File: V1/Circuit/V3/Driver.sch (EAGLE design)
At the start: 40 parts, among them IC1 DRV8303DCA

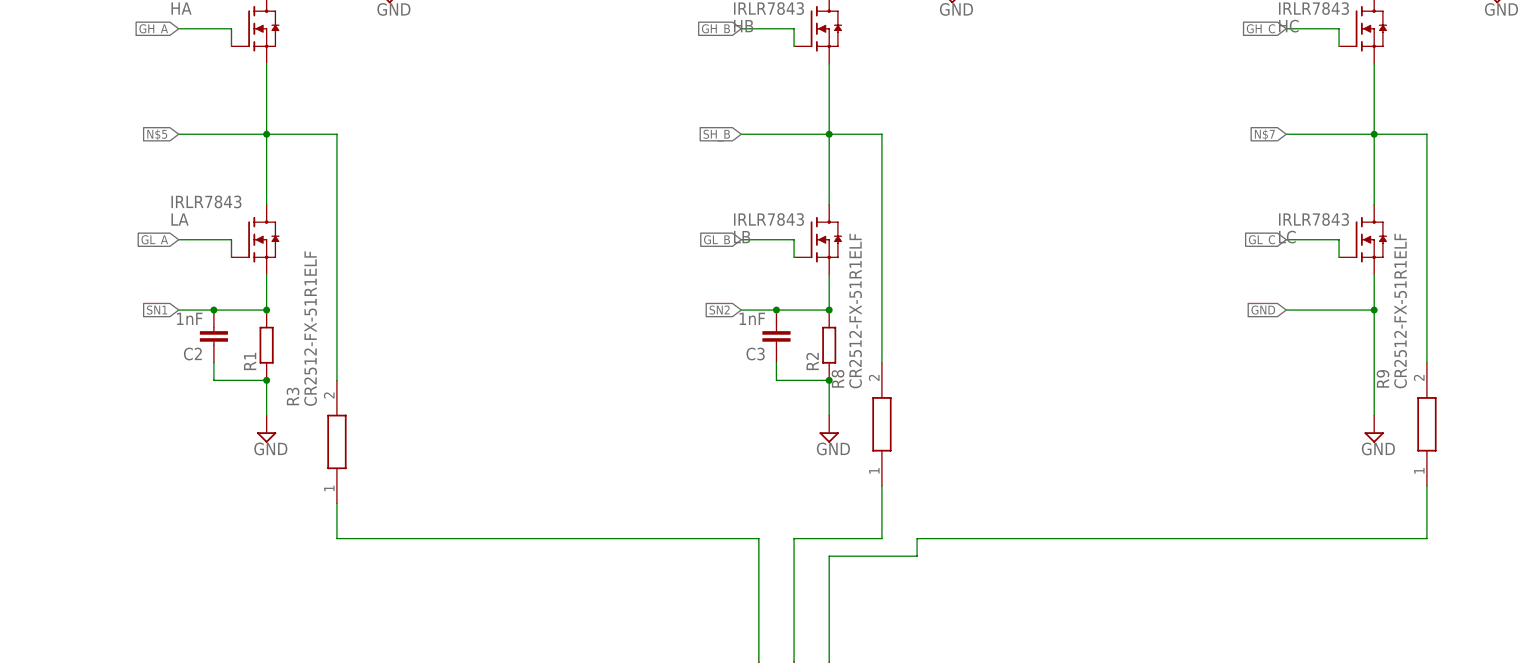
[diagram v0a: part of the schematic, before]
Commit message: Added the FOC library
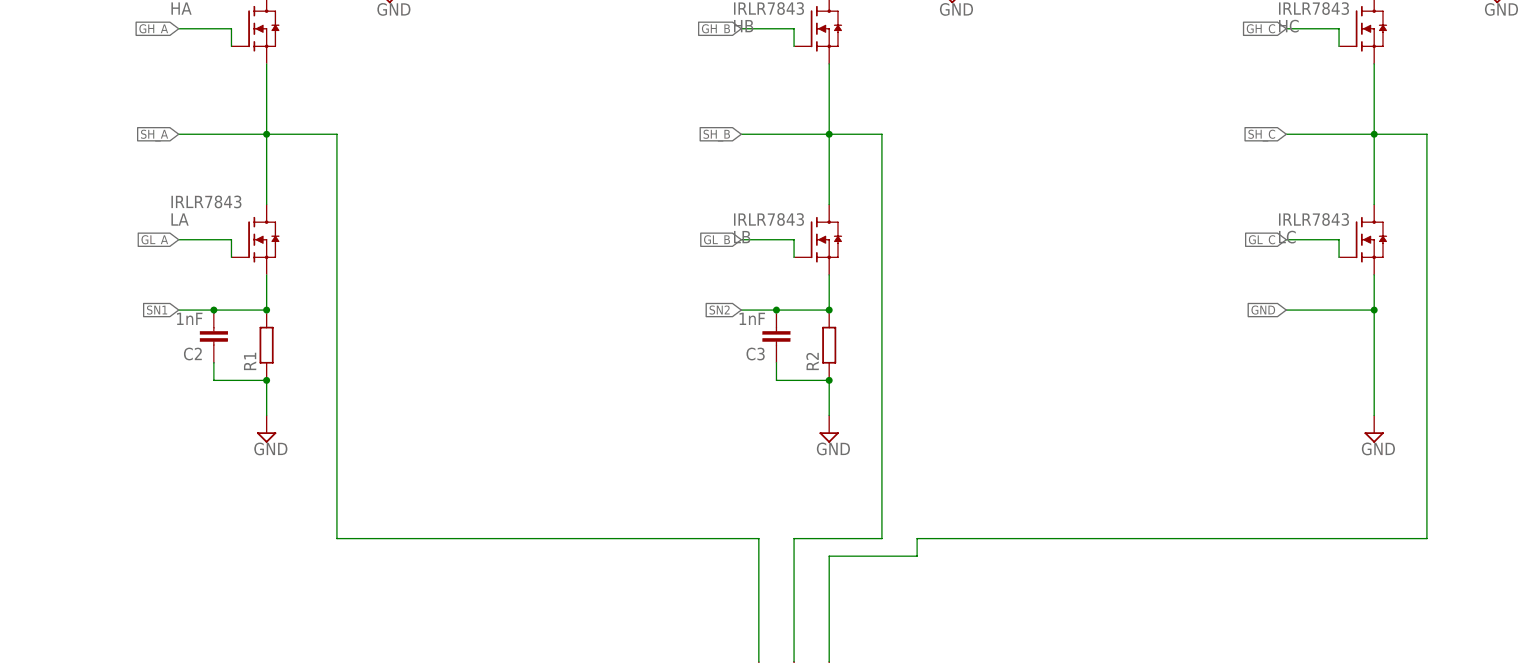
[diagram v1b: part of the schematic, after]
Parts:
- removed R3, R8, R9: CR2512-FX-51R1ELF, CR2512-FX-51R1ELF:CR2512-FX-51R1ELF
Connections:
- removed net N$5: HA.S, LA.D, R3.2
- removed net N$6: B.P, R8.1
- removed net N$7: HC.S, LC.D, R9.2
- net SH_A: now also HA.S, LA.D; no longer R3.1
- net SH_B: now also B.P; no longer R8.2
- net SH_C: now also HC.S, LC.D; no longer R9.1
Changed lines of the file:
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@@
 <part name="SUPPLY24" library="supply2" library_urn="urn:adsk.eagle:library:372" deviceset="GND" device=""/>
 <part name="C16" library="SparkFun-Capacitors" deviceset="2.2NF/2200PF" device="-0603-50V-10%" value="2.2nF"/>
-<part name="R3" library="CR2512-FX-51R1ELF" deviceset="CR2512-FX-51R1ELF" device=""/>
-<part name="R8" library="CR2512-FX-51R1ELF" deviceset="CR2512-FX-51R1ELF" device=""/>
-<part name="R9" library="CR2512-FX-51R1ELF" deviceset="CR2512-FX-51R1ELF" device=""/>
 </parts>
 <sheets>
@@
 <attribute name="NAME" x="194.564" y="91.821" size="1.778" layer="95" font="vector"/>
 <attribute name="VALUE" x="194.564" y="86.741" size="1.778" layer="96" font="vector"/>
-</instance>
-<instance part="R3" gate="G$1" x="162.56" y="-58.42" smashed="yes" rot="R90">
-<attribute name="NAME" x="156.21" y="-44.45" size="1.778" layer="95" rot="R90" align="center-left"/>
-<attribute name="VALUE" x="158.75" y="-44.45" size="1.778" layer="96" rot="R90" align="center-left"/>
-</instance>
-<instance part="R8" gate="G$1" x="241.3" y="-55.88" smashed="yes" rot="R90">
-<attribute name="NAME" x="234.95" y="-41.91" size="1.778" layer="95" rot="R90" align="center-left"/>
-<attribute name="VALUE" x="237.49" y="-41.91" size="1.778" layer="96" rot="R90" align="center-left"/>
-</instance>
-<instance part="R9" gate="G$1" x="320.04" y="-55.88" smashed="yes" rot="R90">
-<attribute name="NAME" x="313.69" y="-41.91" size="1.778" layer="95" rot="R90" align="center-left"/>
-<attribute name="VALUE" x="316.23" y="-41.91" size="1.778" layer="96" rot="R90" align="center-left"/>
 </instance>
 </instances>
@@
 <net name="SH_C" class="0">
 <segment>
+<wire x1="312.42" y1="5.08" x2="312.42" y2="-5.08" width="0.1524" layer="91"/>
+<wire x1="312.42" y1="-5.08" x2="299.72" y2="-5.08" width="0.1524" layer="91"/>
+<label x="299.72" y="-5.08" size="1.27" layer="95" rot="R180" xref="yes"/>
+<wire x1="312.42" y1="-5.08" x2="320.04" y2="-5.08" width="0.1524" layer="91"/>
+<wire x1="320.04" y1="-5.08" x2="320.04" y2="-63.5" width="0.1524" layer="91"/>
 <wire x1="320.04" y1="-63.5" x2="246.38" y2="-63.5" width="0.1524" layer="91"/>
 <wire x1="246.38" y1="-63.5" x2="246.38" y2="-66.04" width="0.1524" layer="91"/>
 <wire x1="246.38" y1="-66.04" x2="233.68" y2="-66.04" width="0.1524" layer="91"/>
 <wire x1="233.68" y1="-66.04" x2="233.68" y2="-81.28" width="0.1524" layer="91"/>
+<junction x="312.42" y="-5.08"/>
+<pinref part="HC" gate="G$1" pin="S"/>
+<pinref part="LC" gate="G$1" pin="D"/>
+<wire x1="312.42" y1="-5.08" x2="312.42" y2="-15.24" width="0.1524" layer="91"/>
 <pinref part="C" gate="1" pin="P"/>
-<wire x1="320.04" y1="-55.88" x2="320.04" y2="-63.5" width="0.1524" layer="91"/>
-<pinref part="R9" gate="G$1" pin="1"/>
 </segment>
 <segment>
@@
 <label x="220.98" y="-5.08" size="1.27" layer="95" rot="R180" xref="yes"/>
 <wire x1="233.68" y1="-5.08" x2="241.3" y2="-5.08" width="0.1524" layer="91"/>
+<wire x1="241.3" y1="-5.08" x2="241.3" y2="-63.5" width="0.1524" layer="91"/>
+<wire x1="241.3" y1="-63.5" x2="228.6" y2="-63.5" width="0.1524" layer="91"/>
+<wire x1="228.6" y1="-63.5" x2="228.6" y2="-81.28" width="0.1524" layer="91"/>
 <junction x="233.68" y="-5.08"/>
 <pinref part="HB" gate="G$1" pin="S"/>
 <pinref part="LB" gate="G$1" pin="D"/>
-<wire x1="241.3" y1="-5.08" x2="241.3" y2="-38.1" width="0.1524" layer="91"/>
-<pinref part="R8" gate="G$1" pin="2"/>
+<pinref part="B" gate="1" pin="P"/>
 </segment>
 <segment>
@@
 <net name="SH_A" class="0">
 <segment>
+<wire x1="152.4" y1="5.08" x2="152.4" y2="-5.08" width="0.1524" layer="91"/>
+<wire x1="152.4" y1="-5.08" x2="152.4" y2="-15.24" width="0.1524" layer="91"/>
+<wire x1="152.4" y1="-5.08" x2="139.7" y2="-5.08" width="0.1524" layer="91"/>
+<label x="139.7" y="-5.08" size="1.27" layer="95" rot="R180" xref="yes"/>
+<wire x1="152.4" y1="-5.08" x2="162.56" y2="-5.08" width="0.1524" layer="91"/>
+<wire x1="162.56" y1="-5.08" x2="162.56" y2="-63.5" width="0.1524" layer="91"/>
 <wire x1="162.56" y1="-63.5" x2="223.52" y2="-63.5" width="0.1524" layer="91"/>
 <wire x1="223.52" y1="-63.5" x2="223.52" y2="-81.28" width="0.1524" layer="91"/>
+<junction x="152.4" y="-5.08"/>
+<pinref part="HA" gate="G$1" pin="S"/>
+<pinref part="LA" gate="G$1" pin="D"/>
 <pinref part="A" gate="1" pin="P"/>
-<wire x1="162.56" y1="-58.42" x2="162.56" y2="-63.5" width="0.1524" layer="91"/>
-<pinref part="R3" gate="G$1" pin="1"/>
 </segment>
 <segment>
@@
 </segment>
 </net>
-<net name="N$5" class="0">
-<segment>
-<pinref part="LA" gate="G$1" pin="D"/>
-<pinref part="HA" gate="G$1" pin="S"/>
-<wire x1="152.4" y1="5.08" x2="152.4" y2="-5.08" width="0.1524" layer="91"/>
-<wire x1="152.4" y1="-5.08" x2="152.4" y2="-15.24" width="0.1524" layer="91"/>
-<wire x1="152.4" y1="-5.08" x2="139.7" y2="-5.08" width="0.1524" layer="91"/>
-<junction x="152.4" y="-5.08"/>
-<wire x1="152.4" y1="-5.08" x2="162.56" y2="-5.08" width="0.1524" layer="91"/>
-<wire x1="162.56" y1="-5.08" x2="162.56" y2="-40.64" width="0.1524" layer="91"/>
-<label x="139.7" y="-5.08" size="1.27" layer="95" rot="R180" xref="yes"/>
-<pinref part="R3" gate="G$1" pin="2"/>
-</segment>
-</net>
-<net name="N$6" class="0">
-<segment>
-<wire x1="241.3" y1="-55.88" x2="241.3" y2="-63.5" width="0.1524" layer="91"/>
-<wire x1="241.3" y1="-63.5" x2="228.6" y2="-63.5" width="0.1524" layer="91"/>
-<wire x1="228.6" y1="-63.5" x2="228.6" y2="-81.28" width="0.1524" layer="91"/>
-<pinref part="B" gate="1" pin="P"/>
-<pinref part="R8" gate="G$1" pin="1"/>
-</segment>
-</net>
-<net name="N$7" class="0">
-<segment>
-<pinref part="LC" gate="G$1" pin="D"/>
-<pinref part="HC" gate="G$1" pin="S"/>
-<wire x1="312.42" y1="5.08" x2="312.42" y2="-5.08" width="0.1524" layer="91"/>
-<wire x1="312.42" y1="-5.08" x2="299.72" y2="-5.08" width="0.1524" layer="91"/>
-<junction x="312.42" y="-5.08"/>
-<wire x1="312.42" y1="-5.08" x2="312.42" y2="-15.24" width="0.1524" layer="91"/>
-<wire x1="312.42" y1="-5.08" x2="320.04" y2="-5.08" width="0.1524" layer="91"/>
-<wire x1="320.04" y1="-5.08" x2="320.04" y2="-38.1" width="0.1524" layer="91"/>
-<label x="299.72" y="-5.08" size="1.27" layer="95" rot="R180" xref="yes"/>
-<pinref part="R9" gate="G$1" pin="2"/>
-</segment>
-</net>

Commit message: Circuit: Added DRV8300, and the Gate Circuit. Haven't added the Not gate
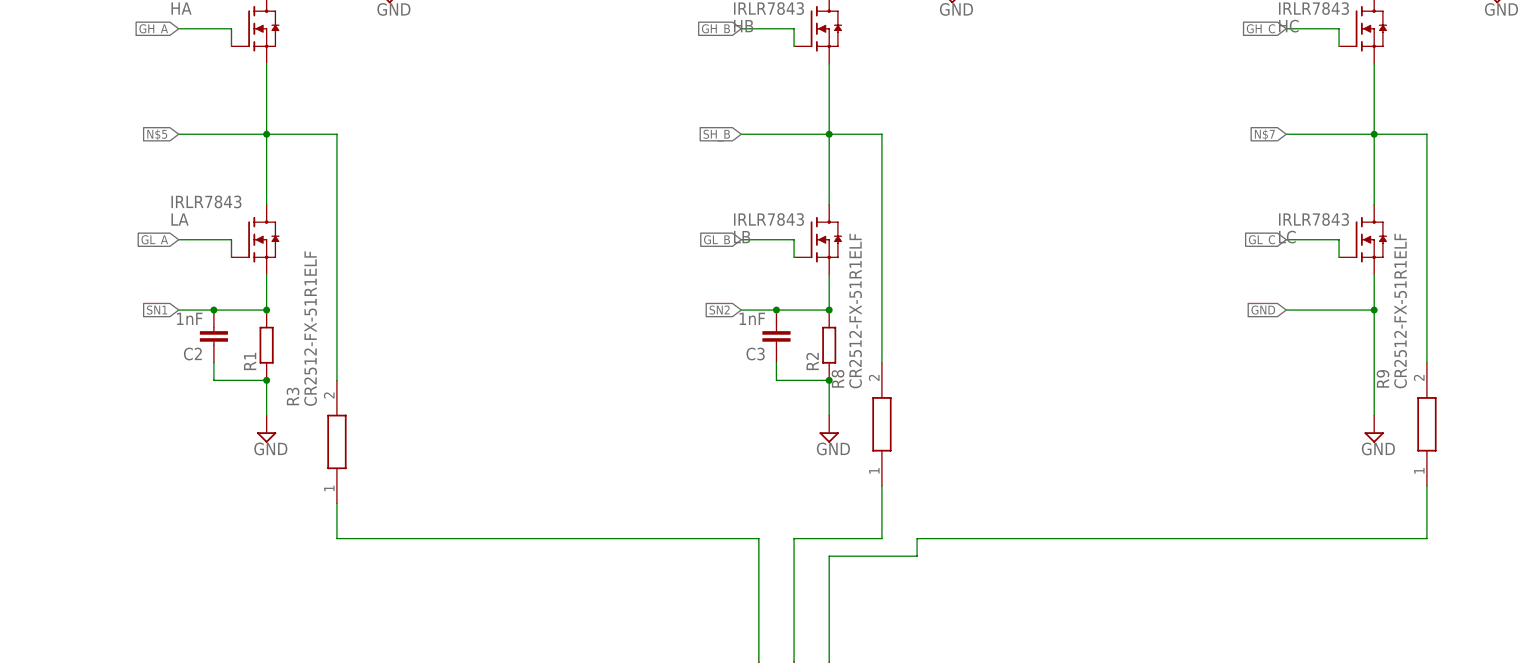
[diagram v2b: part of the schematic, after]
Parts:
- added R3, R8, R9: CR2512-FX-51R1ELF, CR2512-FX-51R1ELF:CR2512-FX-51R1ELF
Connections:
- new net N$5: HA.S, LA.D, R3.2
- new net N$6: B.P, R8.1
- new net N$7: HC.S, LC.D, R9.2
- net SH_A: now also R3.1; no longer HA.S, LA.D
- net SH_B: now also R8.2; no longer B.P
- net SH_C: now also R9.1; no longer HC.S, LC.D
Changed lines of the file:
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@@
 <part name="SUPPLY24" library="supply2" library_urn="urn:adsk.eagle:library:372" deviceset="GND" device=""/>
 <part name="C16" library="SparkFun-Capacitors" deviceset="2.2NF/2200PF" device="-0603-50V-10%" value="2.2nF"/>
+<part name="R3" library="CR2512-FX-51R1ELF" deviceset="CR2512-FX-51R1ELF" device=""/>
+<part name="R8" library="CR2512-FX-51R1ELF" deviceset="CR2512-FX-51R1ELF" device=""/>
+<part name="R9" library="CR2512-FX-51R1ELF" deviceset="CR2512-FX-51R1ELF" device=""/>
 </parts>
 <sheets>
@@
 <attribute name="NAME" x="194.564" y="91.821" size="1.778" layer="95" font="vector"/>
 <attribute name="VALUE" x="194.564" y="86.741" size="1.778" layer="96" font="vector"/>
+</instance>
+<instance part="R3" gate="G$1" x="162.56" y="-58.42" smashed="yes" rot="R90">
+<attribute name="NAME" x="156.21" y="-44.45" size="1.778" layer="95" rot="R90" align="center-left"/>
+<attribute name="VALUE" x="158.75" y="-44.45" size="1.778" layer="96" rot="R90" align="center-left"/>
+</instance>
+<instance part="R8" gate="G$1" x="241.3" y="-55.88" smashed="yes" rot="R90">
+<attribute name="NAME" x="234.95" y="-41.91" size="1.778" layer="95" rot="R90" align="center-left"/>
+<attribute name="VALUE" x="237.49" y="-41.91" size="1.778" layer="96" rot="R90" align="center-left"/>
+</instance>
+<instance part="R9" gate="G$1" x="320.04" y="-55.88" smashed="yes" rot="R90">
+<attribute name="NAME" x="313.69" y="-41.91" size="1.778" layer="95" rot="R90" align="center-left"/>
+<attribute name="VALUE" x="316.23" y="-41.91" size="1.778" layer="96" rot="R90" align="center-left"/>
 </instance>
 </instances>
@@
 <net name="SH_C" class="0">
 <segment>
-<wire x1="312.42" y1="5.08" x2="312.42" y2="-5.08" width="0.1524" layer="91"/>
-<wire x1="312.42" y1="-5.08" x2="299.72" y2="-5.08" width="0.1524" layer="91"/>
-<label x="299.72" y="-5.08" size="1.27" layer="95" rot="R180" xref="yes"/>
-<wire x1="312.42" y1="-5.08" x2="320.04" y2="-5.08" width="0.1524" layer="91"/>
-<wire x1="320.04" y1="-5.08" x2="320.04" y2="-63.5" width="0.1524" layer="91"/>
 <wire x1="320.04" y1="-63.5" x2="246.38" y2="-63.5" width="0.1524" layer="91"/>
 <wire x1="246.38" y1="-63.5" x2="246.38" y2="-66.04" width="0.1524" layer="91"/>
 <wire x1="246.38" y1="-66.04" x2="233.68" y2="-66.04" width="0.1524" layer="91"/>
 <wire x1="233.68" y1="-66.04" x2="233.68" y2="-81.28" width="0.1524" layer="91"/>
-<junction x="312.42" y="-5.08"/>
-<pinref part="HC" gate="G$1" pin="S"/>
-<pinref part="LC" gate="G$1" pin="D"/>
-<wire x1="312.42" y1="-5.08" x2="312.42" y2="-15.24" width="0.1524" layer="91"/>
 <pinref part="C" gate="1" pin="P"/>
+<wire x1="320.04" y1="-55.88" x2="320.04" y2="-63.5" width="0.1524" layer="91"/>
+<pinref part="R9" gate="G$1" pin="1"/>
 </segment>
 <segment>
@@
 <label x="220.98" y="-5.08" size="1.27" layer="95" rot="R180" xref="yes"/>
 <wire x1="233.68" y1="-5.08" x2="241.3" y2="-5.08" width="0.1524" layer="91"/>
-<wire x1="241.3" y1="-5.08" x2="241.3" y2="-63.5" width="0.1524" layer="91"/>
-<wire x1="241.3" y1="-63.5" x2="228.6" y2="-63.5" width="0.1524" layer="91"/>
-<wire x1="228.6" y1="-63.5" x2="228.6" y2="-81.28" width="0.1524" layer="91"/>
 <junction x="233.68" y="-5.08"/>
 <pinref part="HB" gate="G$1" pin="S"/>
 <pinref part="LB" gate="G$1" pin="D"/>
-<pinref part="B" gate="1" pin="P"/>
+<wire x1="241.3" y1="-5.08" x2="241.3" y2="-38.1" width="0.1524" layer="91"/>
+<pinref part="R8" gate="G$1" pin="2"/>
 </segment>
 <segment>
@@
 <net name="SH_A" class="0">
 <segment>
-<wire x1="152.4" y1="5.08" x2="152.4" y2="-5.08" width="0.1524" layer="91"/>
-<wire x1="152.4" y1="-5.08" x2="152.4" y2="-15.24" width="0.1524" layer="91"/>
-<wire x1="152.4" y1="-5.08" x2="139.7" y2="-5.08" width="0.1524" layer="91"/>
-<label x="139.7" y="-5.08" size="1.27" layer="95" rot="R180" xref="yes"/>
-<wire x1="152.4" y1="-5.08" x2="162.56" y2="-5.08" width="0.1524" layer="91"/>
-<wire x1="162.56" y1="-5.08" x2="162.56" y2="-63.5" width="0.1524" layer="91"/>
 <wire x1="162.56" y1="-63.5" x2="223.52" y2="-63.5" width="0.1524" layer="91"/>
 <wire x1="223.52" y1="-63.5" x2="223.52" y2="-81.28" width="0.1524" layer="91"/>
-<junction x="152.4" y="-5.08"/>
-<pinref part="HA" gate="G$1" pin="S"/>
-<pinref part="LA" gate="G$1" pin="D"/>
 <pinref part="A" gate="1" pin="P"/>
+<wire x1="162.56" y1="-58.42" x2="162.56" y2="-63.5" width="0.1524" layer="91"/>
+<pinref part="R3" gate="G$1" pin="1"/>
 </segment>
 <segment>
@@
 </segment>
 </net>
+<net name="N$5" class="0">
+<segment>
+<pinref part="LA" gate="G$1" pin="D"/>
+<pinref part="HA" gate="G$1" pin="S"/>
+<wire x1="152.4" y1="5.08" x2="152.4" y2="-5.08" width="0.1524" layer="91"/>
+<wire x1="152.4" y1="-5.08" x2="152.4" y2="-15.24" width="0.1524" layer="91"/>
+<wire x1="152.4" y1="-5.08" x2="139.7" y2="-5.08" width="0.1524" layer="91"/>
+<junction x="152.4" y="-5.08"/>
+<wire x1="152.4" y1="-5.08" x2="162.56" y2="-5.08" width="0.1524" layer="91"/>
+<wire x1="162.56" y1="-5.08" x2="162.56" y2="-40.64" width="0.1524" layer="91"/>
+<label x="139.7" y="-5.08" size="1.27" layer="95" rot="R180" xref="yes"/>
+<pinref part="R3" gate="G$1" pin="2"/>
+</segment>
+</net>
+<net name="N$6" class="0">
+<segment>
+<wire x1="241.3" y1="-55.88" x2="241.3" y2="-63.5" width="0.1524" layer="91"/>
+<wire x1="241.3" y1="-63.5" x2="228.6" y2="-63.5" width="0.1524" layer="91"/>
+<wire x1="228.6" y1="-63.5" x2="228.6" y2="-81.28" width="0.1524" layer="91"/>
+<pinref part="B" gate="1" pin="P"/>
+<pinref part="R8" gate="G$1" pin="1"/>
+</segment>
+</net>
+<net name="N$7" class="0">
+<segment>
+<pinref part="LC" gate="G$1" pin="D"/>
+<pinref part="HC" gate="G$1" pin="S"/>
+<wire x1="312.42" y1="5.08" x2="312.42" y2="-5.08" width="0.1524" layer="91"/>
+<wire x1="312.42" y1="-5.08" x2="299.72" y2="-5.08" width="0.1524" layer="91"/>
+<junction x="312.42" y="-5.08"/>
+<wire x1="312.42" y1="-5.08" x2="312.42" y2="-15.24" width="0.1524" layer="91"/>
+<wire x1="312.42" y1="-5.08" x2="320.04" y2="-5.08" width="0.1524" layer="91"/>
+<wire x1="320.04" y1="-5.08" x2="320.04" y2="-38.1" width="0.1524" layer="91"/>
+<label x="299.72" y="-5.08" size="1.27" layer="95" rot="R180" xref="yes"/>
+<pinref part="R9" gate="G$1" pin="2"/>
+</segment>
+</net>
